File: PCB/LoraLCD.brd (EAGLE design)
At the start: 124.9 x 83.1 mm, 79 parts, among them IC1 STM32F767ZIT6, IC2 24AA025E64T-I/OT, IC5 TPS613222ADBVR, Q1 SSM3J338R,LF, Q2 SSM3J338R,LF, Q3 SSM3J338R,LF, Q4 SSM3J338R,LF, Q5 SSM3J338R,LF, U1 LORA-868MHZ

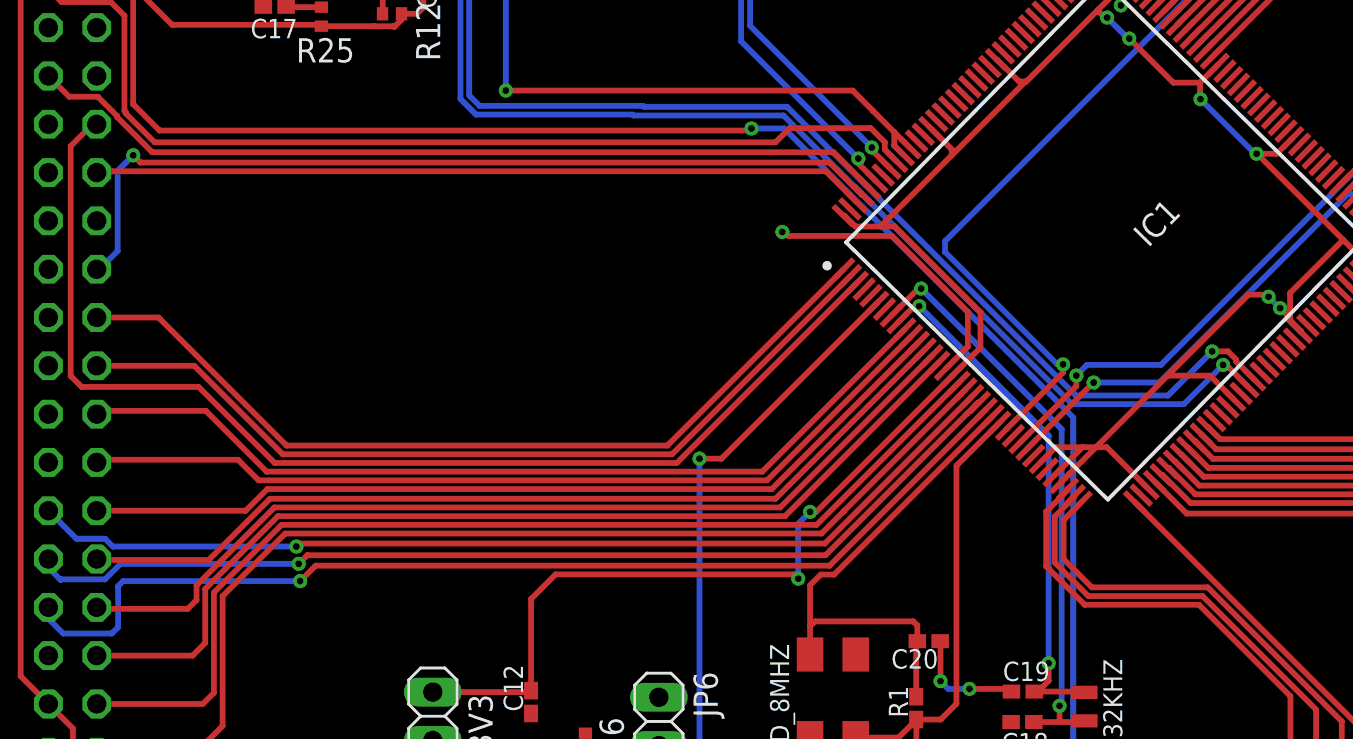
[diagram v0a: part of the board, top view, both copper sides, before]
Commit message: fix 2 pin CS and RTS in control pin for LCD
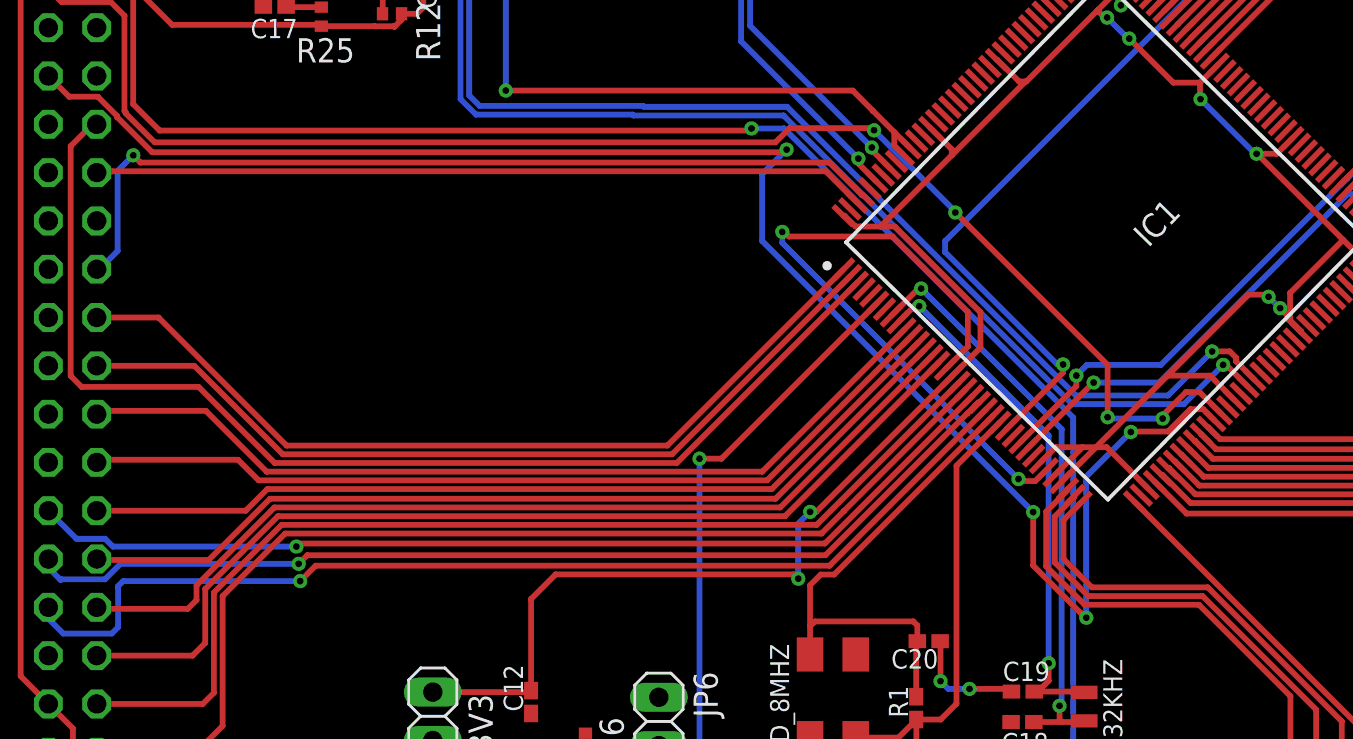
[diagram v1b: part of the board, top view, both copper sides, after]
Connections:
- net CS: now also IC1.49; no longer IC1.140
- net RST: now also IC1.50; no longer IC1.136
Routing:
- net CS: track 45.7 -> 88.7 mm, vias 0 -> 4
- net RST: track 52.7 -> 77.9 mm, vias 0 -> 4
- net GND: track 36.1 -> 56.1 mm, vias 7 -> 8
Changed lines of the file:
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@@
 </layers>
 <board>
+<fusionteam huburn="a.YnVzaW5lc3M6aGF3aGFtYnVyZzE2MA" projecturn="a.YnVzaW5lc3M6aGF3aGFtYnVyZzE2MCMyMDIwMDMxODI3NjA2OTk3Ng" folderUrn="urn:adsk.wipprod:fs.folder:co.goNDv-9XQGeF0P4ml8q09Q" urn="urn:adsk.wipprod:dm.lineage:8bbLFadqTrStlnf7vHqapw"  versionUrn="urn:adsk.wipprod:fs.file:vf.8bbLFadqTrStlnf7vHqapw?version=1" camFileUrn="" camFileVersionUrn="" lastpublishedchangeguid="9738d50b-fed6-b3af-3941-04c7666c3df5"/>
 <plain>
 <wire x1="14.296478125" y1="67.718971875" x2="14.20326875" y2="27.22685625" width="0" layer="20"/>
@@
 <wire x1="66.332071875" y1="46.817253125" x2="67.506709375" y2="47.991890625" width="0.3048" layer="1"/>
 <wire x1="67.506709375" y1="47.991890625" x2="67.506709375" y2="49.826709375" width="0.3048" layer="1"/>
-<wire x1="67.506709375" y1="49.826709375" x2="63.51341875" y2="53.82" width="0.3048" layer="1"/>
-<wire x1="63.51341875" y1="53.82" x2="58.06" y2="53.82" width="0.3048" layer="1"/>
-<wire x1="58.06" y1="53.82" x2="57.85" y2="54.03" width="0.3048" layer="1"/>
+<wire x1="67.506709375" y1="49.826709375" x2="63.54341875" y2="53.79" width="0.3048" layer="1"/>
+<wire x1="63.54341875" y1="53.79" x2="58.09" y2="53.79" width="0.3048" layer="1"/>
+<wire x1="58.09" y1="53.79" x2="57.85" y2="54.03" width="0.3048" layer="1"/>
 <wire x1="57.85" y1="54.03" x2="57.75" y2="54.03" width="0.3048" layer="1"/>
 <via x="57.75" y="54.03" extent="1-16" drill="0.35"/>
@@
 <vertex x="14.07" y="59.95"/>
 </polygon>
+<wire x1="71.68145" y1="41.56043125" x2="71.05101875" y2="40.93" width="0.3048" layer="1"/>
+<wire x1="71.05101875" y1="40.93" x2="70.22" y2="40.93" width="0.3048" layer="1"/>
+<wire x1="70.22" y1="40.93" x2="70.16925625" y2="40.98074375" width="0.3048" layer="1"/>
+<wire x1="70.16925625" y1="40.98074375" x2="70.16925625" y2="41.03925625" width="0.3048" layer="1"/>
+<via x="70.16925625" y="41.03925625" extent="1-16" drill="0.35"/>
+<wire x1="70.16925625" y1="41.03925625" x2="57.75" y2="53.4585125" width="0.3048" layer="16"/>
+<wire x1="57.75" y1="53.4585125" x2="57.75" y2="54.03" width="0.3048" layer="16"/>
 </signal>
 <signal name="TCS">
@@
 </signal>
 <signal name="CS">
-<contactref element="IC1" pad="140"/>
 <contactref element="LCD" pad="12"/>
-<wire x1="62.359978125" y1="56.311921875" x2="60.4519" y2="58.22" width="0.3048" layer="1"/>
-<wire x1="60.4519" y1="58.22" x2="24.62" y2="58.22" width="0.3048" layer="1"/>
 <wire x1="22.7668" y1="60.0732" x2="22.7668" y2="60.1318875" width="0.3048" layer="1"/>
 <wire x1="22.7668" y1="60.1318875" x2="21.7586875" y2="61.14" width="0.3048" layer="1"/>
 <wire x1="20.25" y1="61.14" x2="19.16" y2="62.23" width="0.3048" layer="1"/>
-<wire x1="24.62" y1="58.22" x2="22.7668" y2="60.0732" width="0.3048" layer="1"/>
+<wire x1="22.7668" y1="60.0732" x2="24.62" y2="58.22" width="0.3048" layer="1"/>
 <wire x1="21.7586875" y1="61.14" x2="20.25" y2="61.14" width="0.3048" layer="1"/>
+<contactref element="IC1" pad="49"/>
+<wire x1="24.62" y1="58.22" x2="57.8359125" y2="58.22" width="0.3048" layer="1"/>
+<wire x1="57.8359125" y1="58.22" x2="57.9761125" y2="58.3602" width="0.3048" layer="1"/>
+<via x="57.9761125" y="58.3602" extent="1-16" drill="0.35"/>
+<wire x1="80.48138125" y1="44.112196875" x2="79.883578125" y2="44.71" width="0.3048" layer="1"/>
+<wire x1="79.883578125" y1="44.71" x2="79.20891875" y2="44.71" width="0.3048" layer="1"/>
+<via x="76.08" y="43.51" extent="1-16" drill="0.35"/>
+<wire x1="76.104" y1="43.534" x2="76.08" y2="43.51" width="0.3048" layer="1"/>
+<wire x1="78.03291875" y1="43.534" x2="76.104" y2="43.534" width="0.3048" layer="1"/>
+<wire x1="79.20891875" y1="44.71" x2="78.03291875" y2="43.534" width="0.3048" layer="1"/>
+<wire x1="76.08" y1="43.51" x2="73.733" y2="41.163" width="0.3048" layer="16"/>
+<wire x1="73.733" y1="41.163" x2="73.733" y2="33.7426" width="0.3048" layer="16"/>
+<via x="73.733" y="33.7426" extent="1-16" drill="0.35"/>
+<via x="70.9426" y="39.3" extent="1-16" drill="0.35"/>
+<wire x1="73.733" y1="33.7426" x2="73.5072" y2="33.9684" width="0.3048" layer="1"/>
+<wire x1="73.5072" y1="33.9684" x2="73.46185625" y2="33.9684" width="0.3048" layer="1"/>
+<wire x1="73.46185625" y1="33.9684" x2="70.9426" y2="36.48765625" width="0.3048" layer="1"/>
+<wire x1="70.9426" y1="36.48765625" x2="70.9426" y2="39.3" width="0.3048" layer="1"/>
+<wire x1="70.9426" y1="39.3" x2="56.69" y2="53.5526" width="0.3048" layer="16"/>
+<wire x1="56.69" y1="53.5526" x2="56.69" y2="57.08" width="0.3048" layer="16"/>
+<wire x1="56.69" y1="57.08" x2="57.9702" y2="58.3602" width="0.3048" layer="16"/>
+<wire x1="57.9702" y1="58.3602" x2="57.9761125" y2="58.3602" width="0.3048" layer="16"/>
 </signal>
 <signal name="N$53">
@@
 <via x="80.35238125" y="47.74761875" extent="1-16" drill="0.35"/>
 <wire x1="82.584109375" y1="46.251946875" x2="81.613" y2="47.22305625" width="0.3048" layer="1"/>
-<wire x1="81.613" y1="47.22305625" x2="81.613" y2="47.3229125" width="0.3048" layer="1"/>
-<wire x1="81.613" y1="47.3229125" x2="81.18829375" y2="47.74761875" width="0.3048" layer="1"/>
-<wire x1="81.18829375" y1="47.74761875" x2="80.35238125" y2="47.74761875" width="0.3048" layer="1"/>
+<wire x1="81.613" y1="47.22305625" x2="81.613" y2="47.4129125" width="0.3048" layer="1"/>
+<wire x1="81.613" y1="47.4129125" x2="81.27829375" y2="47.74761875" width="0.3048" layer="1"/>
+<wire x1="81.27829375" y1="47.74761875" x2="80.35238125" y2="47.74761875" width="0.3048" layer="1"/>
 <wire x1="80.35238125" y1="47.74761875" x2="78.0319625" y2="45.4272" width="0.3048" layer="16"/>
 <wire x1="78.0319625" y1="45.4272" x2="73.1859625" y2="45.4272" width="0.3048" layer="16"/>
@@
 </signal>
 <signal name="RST">
-<contactref element="IC1" pad="136"/>
 <contactref element="LCD" pad="8"/>
 <wire x1="23.224" y1="60.26258125" x2="23.224" y2="60.32126875" width="0.3048" layer="1"/>
@@
 <wire x1="19.85" y1="66.12" x2="19.16" y2="66.81" width="0.3048" layer="1"/>
 <wire x1="19.16" y1="66.81" x2="19.16" y2="67.31" width="0.3048" layer="1"/>
-<wire x1="63.761796875" y1="57.738421875" x2="63.13953125" y2="58.3606875" width="0.3048" layer="1"/>
-<wire x1="63.13953125" y1="58.3606875" x2="63.13953125" y2="58.74944375" width="0.3048" layer="1"/>
-<wire x1="63.13953125" y1="58.74944375" x2="62.398975" y2="59.49" width="0.3048" layer="1"/>
 <wire x1="58.14" y1="59.49" x2="57.39" y2="58.74" width="0.3048" layer="1"/>
 <wire x1="57.39" y1="58.74" x2="24.74658125" y2="58.74" width="0.3048" layer="1"/>
-<wire x1="62.398975" y1="59.49" x2="58.14" y2="59.49" width="0.3048" layer="1"/>
+<wire x1="58.14" y1="59.49" x2="62.45846875" y2="59.49" width="0.3048" layer="1"/>
 <wire x1="24.74658125" y1="58.74" x2="23.224" y2="60.26258125" width="0.3048" layer="1"/>
+<contactref element="IC1" pad="50"/>
+<wire x1="62.45846875" y1="59.49" x2="62.5731375" y2="59.37533125" width="0.3048" layer="1"/>
+<via x="62.5731375" y="59.37533125" extent="1-16" drill="0.35"/>
+<wire x1="62.5731375" y1="59.37533125" x2="66.84854375" y2="55.099925" width="0.3048" layer="16"/>
+<wire x1="66.84854375" y1="55.099925" x2="66.84854375" y2="55.05145625" width="0.3048" layer="16"/>
+<via x="66.84854375" y="55.05145625" extent="1-16" drill="0.35"/>
+<wire x1="66.84854375" y1="55.05145625" x2="74.85626875" y2="47.04373125" width="0.3048" layer="1"/>
+<wire x1="74.85626875" y1="47.04373125" x2="74.85626875" y2="44.287" width="0.3048" layer="1"/>
+<via x="74.85626875" y="44.287" extent="1-16" drill="0.35"/>
+<wire x1="77.750003125" y1="44.217" x2="74.92626875" y2="44.217" width="0.3048" layer="16"/>
+<wire x1="74.85626875" y1="44.287" x2="74.92626875" y2="44.217" width="0.3048" layer="16"/>
+<via x="77.750003125" y="44.217" extent="1-16" drill="0.35"/>
+<wire x1="79.69065625" y1="45.61" x2="80.831834375" y2="44.468821875" width="0.3048" layer="1"/>
+<wire x1="78.98" y1="45.61" x2="77.750003125" y2="44.380003125" width="0.3048" layer="1"/>
+<wire x1="77.750003125" y1="44.217" x2="77.750003125" y2="44.380003125" width="0.3048" layer="1"/>
+<wire x1="78.98" y1="45.61" x2="79.69065625" y2="45.61" width="0.3048" layer="1"/>
 </signal>
 <signal name="3V3">
